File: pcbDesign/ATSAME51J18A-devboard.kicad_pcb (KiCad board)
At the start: 2 copper layers, 68 parts, among them J1 Micro_SD_Card, J2 S2B-ZR-SM4A-TF(LF)(SN), J3 SM04B-SRSS-TB(LF)(SN), J4 Conn_01x25, J5 Conn_01x01_Male, J6 Conn_01x02_Male, J7 Conn_01x06_Male, J8 Conn_01x25, J9 12401598E4-2A, U1 TCAN1051GVDRQ1, U2 ATSAME51J18A-A, U3 MIC5219-5.0YMM, U4 LM27762, U5 LM2775QDSGTQ1, U6 SC630AULTRT, U7 BQ24074RGT, U8 BQ27441DRZR-G1B, Y1 32.768

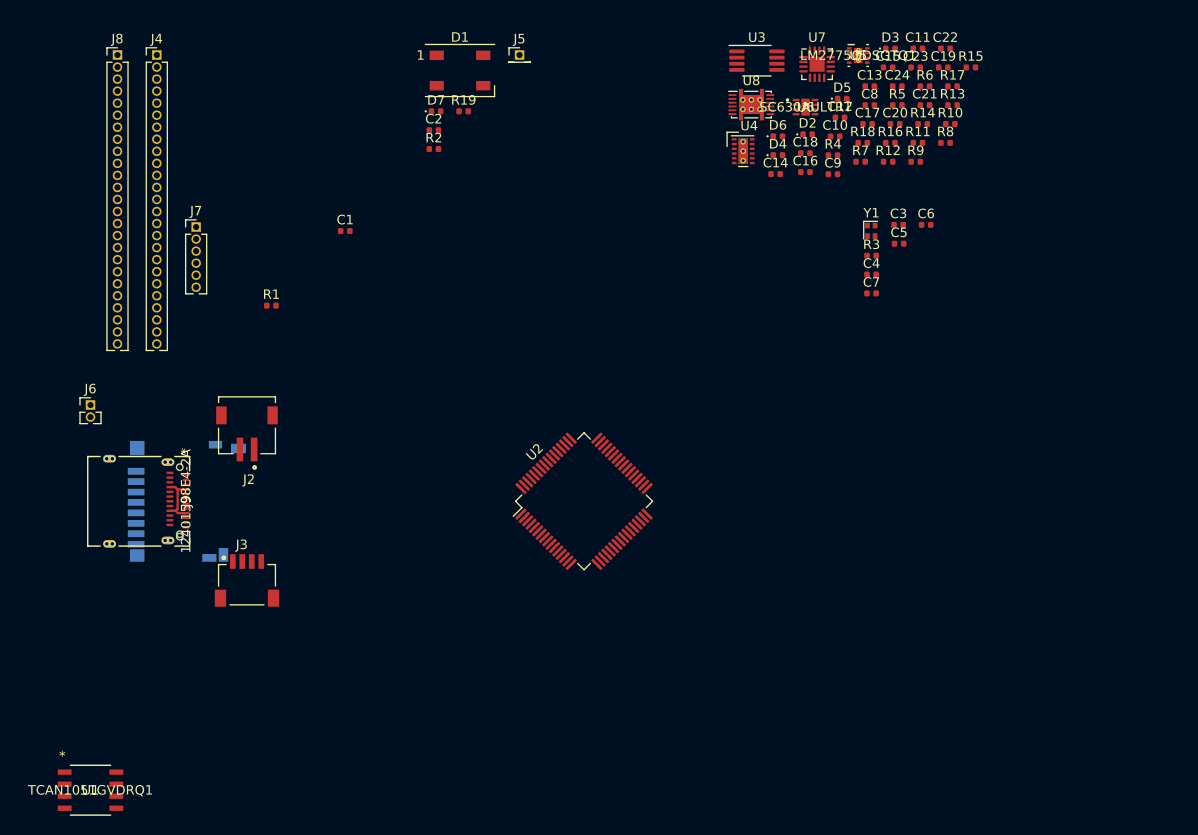
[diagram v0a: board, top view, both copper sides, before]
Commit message: Fixed power rail enabling systems and rearanged pins for easier use
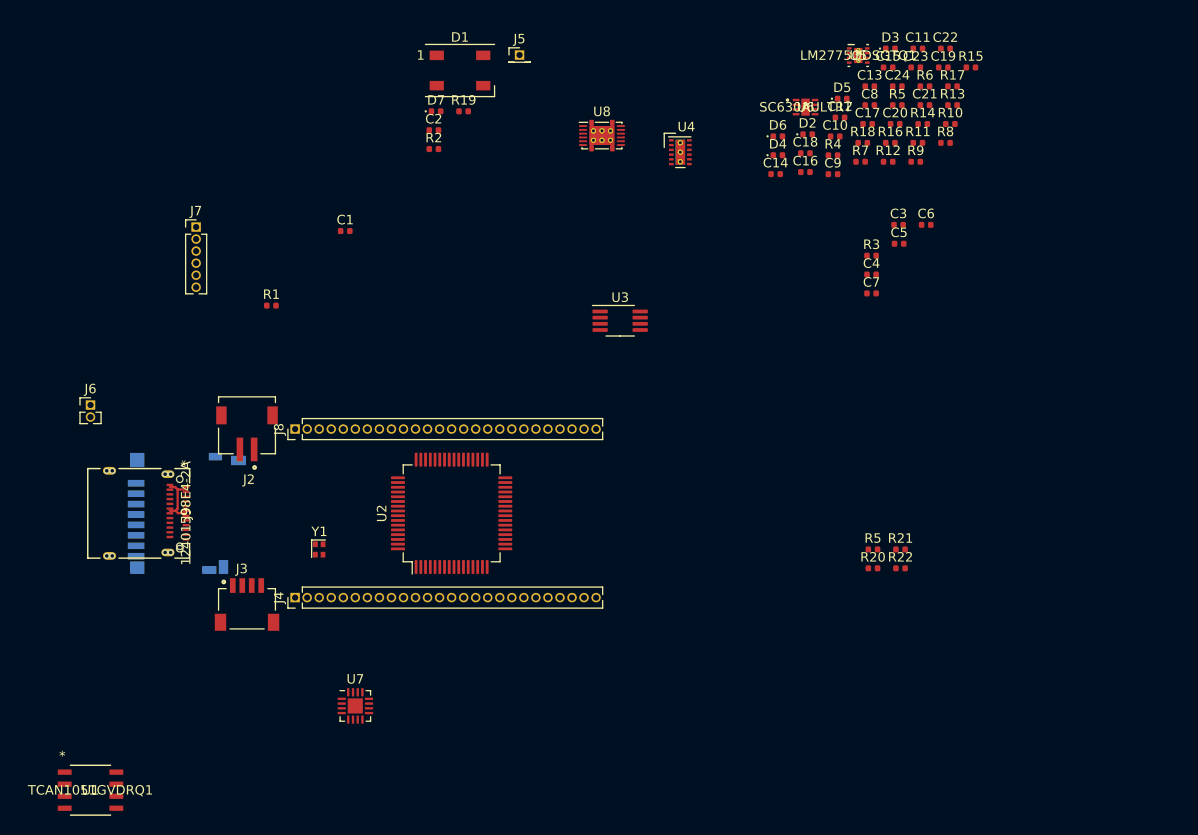
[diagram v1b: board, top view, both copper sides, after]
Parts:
- added R20: 10k, Resistor_SMD:R_0402_1005Metric, F.Cu at (193.0, 132.8)
- added R21: 10k, Resistor_SMD:R_0402_1005Metric, F.Cu at (195.9, 130.8)
- added R22: 10k, Resistor_SMD:R_0402_1005Metric, F.Cu at (195.9, 132.8)
- added R5: 10k, Resistor_SMD:R_0402_1005Metric, F.Cu at (193.0, 130.8)
- C17, C21: value C -> 2.2u
- J2: value S2B-ZR-SM4A-TF(LF)(SN) -> BAT
- J3: value SM04B-SRSS-TB(LF)(SN) -> QWIIC
- J4: value Conn_01x25 -> L_PINS; footprint Connector_PinHeader_1.27mm:PinHeader_1x25_P1.27mm_Vertical -> Connector_PinHeader_1.27mm:PinHeader_1x26_P1.27mm_Vertical
- J5: value Conn_01x01_Male -> NP_OUT
- J6: value Conn_01x02_Male -> USB
- J7: value Conn_01x06_Male -> QSPI
- J8: value Conn_01x25 -> R_PINS; footprint Connector_PinHeader_1.27mm:PinHeader_1x25_P1.27mm_Vertical -> Connector_PinHeader_1.27mm:PinHeader_1x26_P1.27mm_Vertical
- U2: value ATSAME51J18A-A -> ATSAME51JXXA-A
- moved U7 83.4 mm to (138.4, 147.3)
- moved Y1 67.2 mm to (134.6, 130.8)
- moved J4 59.1 mm to (132.1, 135.9), turned to 90 degrees
- moved J8 43.7 mm to (132.1, 118.1), turned to 90 degrees
- moved U3 31.0 mm to (166.4, 106.7)
- moved U8 16.1 mm to (164.4, 87.1)
- moved U2 14.0 mm to (148.6, 127.0), turned to 90 degrees
- moved U4 6.63 mm to (172.7, 88.9)
- moved J3 2.54 mm to (127.0, 134.6)
- moved J1 1.27 mm to (120.7, 127.0)
- moved J9 1.27 mm to (115.6, 127.0)
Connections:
- J4 pad 10: 7[I2SWS] -> 6[I2SSCK]
- J4 pad 11: 10[I2SDO] -> 7[I2SWS]
- J4 pad 12: 11[I2SDI] -> 10[I2SDO]
- J4 pad 13: 14[I2SMCLK] -> 11[I2SDI]
- J4 pad 14: 15 -> 14[I2SMCLK]
- J4 pad 15: 18 -> 15
- J4 pad 16: 19 -> 18
- J4 pad 17: 22 -> 19
- J4 pad 18: 23 -> 22
- J4 pad 19: 26 -> 23
- J4 pad 2: RST -> GND
- J4 pad 20: 27 -> 26
- J4 pad 21: 30[Rx1] -> 27
- J4 pad 22: 31[Tx1] -> 30[Rx1]
- J4 pad 23: VBUS_3V3_CH1_REG -> 31[Tx1]
- J4 pad 24: GND -> VBUS_3V3_CH1_REG
- J4 pad 25: VBUS_-3V3_CH2_REG -> GND
- J4 pad 3: CHRG -> RST
- J4 pad 4: VBUS_3V3_CH1_REG -> CHRG
- J4 pad 5: GND -> VBUS_3V3_CH1_REG
- J4 pad 6: VBUS_-3V3_CH2_REG -> GND
- J4 pad 7: 2[SDA] -> VBUS_-3V3_CH2_REG
- J4 pad 8: 3[SCL] -> 2[SDA]
- J4 pad 9: 6[I2SSCK] -> 3[SCL]
- J8 pad 10: 5[MO] -> 4[SCK]
- J8 pad 11: 8[MI] -> 5[MO]
- J8 pad 12: 9[CS] -> 8[MI]
- J8 pad 13: 12 -> 9[CS]
- J8 pad 14: 13 -> 12
- J8 pad 15: 16 -> 13
- J8 pad 16: 17 -> 16
- J8 pad 17: 20 -> 17
- J8 pad 18: 21 -> 20
- J8 pad 19: 24 -> 21
- J8 pad 2: VBUS_VIN_NREG -> GND
- J8 pad 20: 25 -> 24
- J8 pad 21: 28[CANH] -> 25
- J8 pad 22: 29[CANL] -> 28[CANH]
- J8 pad 23: VBUS_3V3_CH1_REG -> 29[CANL]
- J8 pad 24: GND -> VBUS_3V3_CH1_REG
- J8 pad 25: VBUS_-3V3_CH2_REG -> GND
- J8 pad 3: AREF -> VBUS_VIN_NREG
- J8 pad 4: VBUS_3V3_CH1_REG -> AREF
- J8 pad 5: GND -> VBUS_3V3_CH1_REG
- J8 pad 6: VBUS_-3V3_CH2_REG -> GND
- J8 pad 7: 0[Rx0] -> VBUS_-3V3_CH2_REG
- J8 pad 8: 1[Tx0] -> 0[Rx0]
- J8 pad 9: 4[SCK] -> 1[Tx0]

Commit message: Changed pin pitch to 2.54mm
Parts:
- removed the R5 at (195.6, 83.9)
- added J10: CAN, SM04B-SRSS-TB_LF__SN_:JST_SM04B-SRSS-TB(LF)(SN), F.Cu at (135.9, 134.6)
- J4, J8: footprint Connector_PinHeader_1.27mm:PinHeader_1x26_P1.27mm_Vertical -> Connector_PinSocket_2.54mm:PinSocket_1x26_P2.54mm_Vertical
- J5: footprint Connector_PinHeader_1.27mm:PinHeader_1x01_P1.27mm_Vertical -> Connector_PinSocket_2.54mm:PinSocket_1x01_P2.54mm_Vertical
- J6: footprint Connector_PinHeader_1.27mm:PinHeader_1x02_P1.27mm_Vertical -> Connector_PinSocket_2.54mm:PinSocket_1x02_P2.54mm_Vertical
- J7: footprint Connector_PinHeader_1.27mm:PinHeader_1x06_P1.27mm_Vertical -> Connector_PinSocket_2.54mm:PinSocket_1x06_P2.54mm_Vertical
- U2: value ATSAME51JXXA-A -> ATSAME51J18A-A
- moved J4 10.2 mm to (142.2, 135.9)
- moved J8 10.2 mm to (142.2, 118.1)
- moved J2 8.89 mm to (135.9, 118.1)
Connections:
- D6 pad 2: VBUS_BAT_NREG -> (no net)
- J4 pad 10: 6[I2SSCK] -> (no net)
- J4 pad 11: 7[I2SWS] -> (no net)
- J4 pad 15: 15 -> (no net)
- J4 pad 22: 30[Rx1] -> (no net)
- J4 pad 23: 31[Tx1] -> (no net)
- J9 pad A10: Net-(J9-PadA10) -> (no net)
- J9 pad A11: Net-(J9-PadA11) -> (no net)
- J9 pad A2: Net-(J9-PadA2) -> (no net)
- J9 pad A3: Net-(J9-PadA3) -> (no net)
- J9 pad A8: Net-(J9-PadA8) -> (no net)
- J9 pad B10: Net-(J9-PadB10) -> (no net)
- J9 pad B11: Net-(J9-PadB11) -> (no net)
- J9 pad B2: Net-(J9-PadB2) -> (no net)
- J9 pad B3: Net-(J9-PadB3) -> (no net)
- J9 pad B8: Net-(J9-PadB8) -> (no net)
- U2 pad 15: SDCD -> (no net)
- U2 pad 16: SDWP -> (no net)
- U2 pad 3: 30 -> (no net)
- U2 pad 39: 6[I2SCK] -> (no net)
- U2 pad 41: 15[I2SFS] -> (no net)
- U2 pad 44: 31 -> (no net)
- U2 pad 55: Net-(U2-Pad55) -> (no net)
- U2 pad 57: SWCLK -> (no net)
- U2 pad 58: SWDIO -> (no net)
- U2 pad 59: SWO -> (no net)
- U7 pad 1: Net-(U7-Pad1) -> (no net)
- U7 pad 15: Net-(U7-Pad15) -> (no net)
- U7 pad 7: Net-(U7-Pad7) -> (no net)

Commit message: Finnished routing
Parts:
- added D8: PWR, LED_SMD:LED_0402_1005Metric, F.Cu at (153.7, 127.0)
- added D9: CHRG, LED_SMD:LED_0402_1005Metric, F.Cu at (153.7, 126.0)
- added R23: 10k, Resistor_SMD:R_0402_1005Metric, F.Cu at (155.7, 127.0)
- added R24: 10k, Resistor_SMD:R_0402_1005Metric, F.Cu at (155.7, 126.0)
- C10, C11, C12, C13, C14, C15, C16, C17, C18, C19, C20, C21, C22, C23, C24, C8, C9, D2, D3, D5, J10, J3, R10, R11, R12, R13, R14, R15, R16, R17, R18, R20, R21, R22, R4, R5, R6, R7, R8, R9, U3, U4, U5, U6, U7, U8: moved to B.Cu
- J1: moved to F.Cu
- J9: value 12401598E4-2A -> USB4105_REVA; footprint usb_c:12401598E4-2A -> USB4105_REVA:GCT_USB4105_REVA
- Y1: footprint Oscillator:Oscillator_SMD_Abracon_ASCO-4Pin_1.6x1.2mm -> Crystal:Crystal_SMD_2012-2Pin_2.0x1.2mm
- moved J6 97.9 mm to (206.2, 136.1), turned to 270 degrees
- moved U1 84.1 mm to (187.2, 121.7), turned to 90 degrees
- moved J1 80.0 mm to (200.7, 127.0)
- moved J3 76.3 mm to (203.2, 131.1), turned to 270 degrees
- moved J7 75.0 mm to (193.5, 118.1), turned to 90 degrees
- moved C22 73.3 mm to (154.3, 134.7), turned to 270 degrees
- moved J5 73.3 mm to (201.2, 136.1), turned to 180 degrees
- moved J10 68.2 mm to (203.2, 123.4), turned to 270 degrees
- moved R13 67.8 mm to (150.5, 128.7), turned to 180 degrees
- moved R17 66.9 mm to (148.6, 122.9), turned to 180 degrees
- moved D3 65.7 mm to (158.9, 133.0)
- moved D1 64.6 mm to (187.7, 132.3), turned to 180 degrees
- moved R11 64.6 mm to (149.9, 131.2)
- moved C23 63.7 mm to (154.3, 126.7), turned to 90 degrees
- moved R15 62.2 mm to (156.8, 121.2)
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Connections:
- net GPOUT_PIN renamed VBUS_3V3_CH0_REG
- net USB_DM renamed USB_N
- net USB_DP renamed USB_P
- C22 pad 1: Net-(C22-Pad1) -> VBUS_BAT_NREG
- D6 pad 2: (no net) -> VBUS_BAT_NREG
- J4 pad 10: (no net) -> 6[I2SSCK]
- J4 pad 11: (no net) -> 7[I2SWS]
- J4 pad 15: (no net) -> 15
- J4 pad 22: (no net) -> 30
- J4 pad 23: (no net) -> 31
- R1 pad 1: Net-(J9-PadA5) -> GND
- R1 pad 2: GND -> Net-(J9-PadA5)
- R19 pad 1: LED_PIN -> 13
- U2 pad 26: 13 -> 15
- U2 pad 3: (no net) -> 30
- U2 pad 39: (no net) -> 6[I2SSCK]
- U2 pad 41: (no net) -> 7[I2SWS]
- U2 pad 44: (no net) -> 31
- U2 pad 60: LED_PIN -> 13
- U7 pad 10: Net-(C22-Pad1) -> VBUS_BAT_NREG
- U7 pad 11: Net-(C22-Pad1) -> VBUS_BAT_NREG
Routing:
- net GND: track 0.00 -> 408.1 mm, vias 0 -> 28
- net VBUS_3V3_CH0_REG: track 0.00 -> 156.7 mm, vias 0 -> 5
- net VBUS_3V3_CH1_REG: track 0.00 -> 142.2 mm, vias 0 -> 2
- net VBUS_-3V3_CH2_REG: track 0.00 -> 128.0 mm, vias 0 -> 1
- net EN: track 0.00 -> 123.5 mm, vias 0 -> 3
- net USB_N: track 0.00 -> 121.8 mm, vias 0 -> 6
- net VBUS_NREG: track 0.00 -> 104.1 mm, vias 0 -> 9
- net 2[SDA]: track 0.00 -> 103.5 mm, vias 0 -> 6
- net 3[SCL]: track 0.00 -> 95.4 mm, vias 0 -> 3
- net USB_P: track 0.00 -> 89.6 mm, vias 0 -> 4
- net VBUS_VIN_NREG: track 0.00 -> 86.9 mm
- net 31: track 0.00 -> 57.3 mm, vias 0 -> 3
- net 0[Rx0]: track 0.00 -> 57.2 mm, vias 0 -> 5
- net QDAT2: track 0.00 -> 55.0 mm
- net QDAT1: track 0.00 -> 51.9 mm
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- added copper zone on B.Cu, net GND
- added copper zone on F.Cu, net GND
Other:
- board outline added: 67.3 x 29.2 mm
- net class Default: clearance 0.2 -> 0.127; trace_width 0.25 -> 0.2
- net class Power added: clearance 0.127, trace_width 0.4, via_dia 0.8, via_drill 0.4
- rule trace_clearance: 0.2 -> 0.127
- rule trace_min: 0.2 -> 0.127

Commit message: Labeled pins done
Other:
- board text added: "-3V3"
- board text added: "-3v3"
- board text added: "0"
- board text added: "1"
- board text added: "10"
- board text added: "11"
- board text added: "12"
- board text added: "13"
- board text added: "14"
- board text added: "15"
- board text added: "16"
- board text added: "17"
- board text added: "18"
- board text added: "19"
- board text added: "2"
- board text added: "20"
- board text added: "21"
- board text added: "22"
- board text added: "23"
- board text added: "24"
- board text added: "25"
- board text added: "26"
- board text added: "27"
- board text added: "28"
- board text added: "29"
- board text added: "3"
- board text added: "30"
- board text added: "31"
- board text added: "3V3"
- board text added: "4"
- board text added: "5"
- board text added: "6"
- board text added: "7"
- board text added: "8"
- board text added: "9"
- board text added: "AREF"
- board text added: "BAT"
- board text added: "CANH"
- board text added: "CANL"
- board text added: "CHRG"
- board text added: "CS"
- board text added: "EN"
- board text added: "GND"
- board text added: "I2SDI"
- board text added: "I2SDO"
- board text added: "I2SMCLK"
- board text added: "I2SSCK"
- board text added: "I2SWS"
- board text added: "MI"
- board text added: "MO"
- board text added: "NPO"
- board text added: "QCS"
- board text added: "QD0"
- board text added: "QD1"
- board text added: "QD2"
- board text added: "QD3"
- board text added: "QSCK"
- board text added: "RST"
- board text added: "RX"
- board text added: "SCK"
- board text added: "SCL"
- board text added: "SDA"
- board text added: "TX"
- board text added: "USB+"
- board text added: "USB-"
- board text added: "VIN"

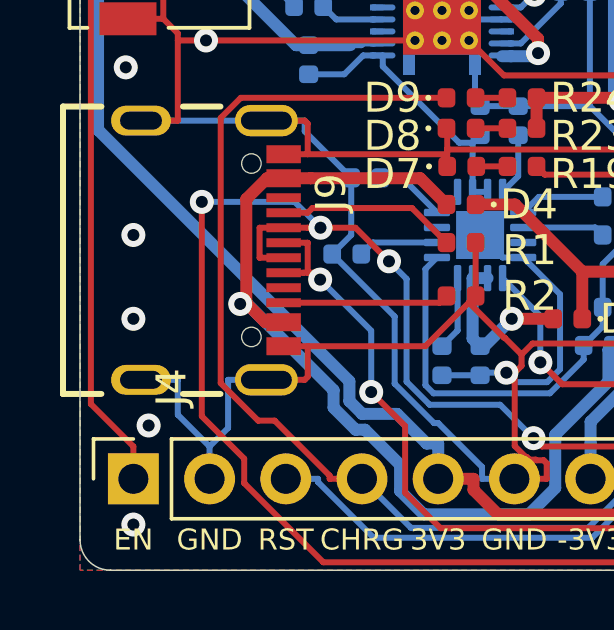
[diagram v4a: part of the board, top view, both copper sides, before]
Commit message: Repanelized board after adding pin descriptions
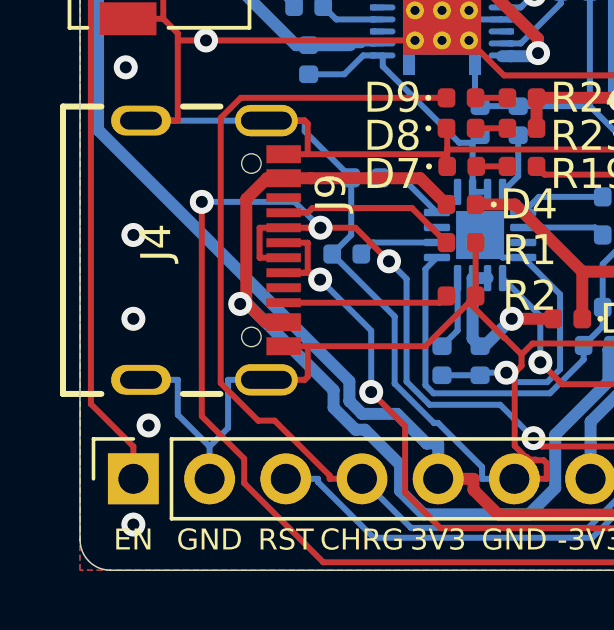
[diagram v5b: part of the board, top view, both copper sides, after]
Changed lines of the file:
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@@
-(kicad_pcb (version 20171130) (host pcbnew "(5.1.6)-1")
+(kicad_pcb (version 20171130) (host pcbnew 5.1.5+dfsg1-2build2)
   (general
     (thickness 1.6)
@@
   (page A4)
   (layers
-    (0 F.Cu signal)
-    (31 B.Cu signal)
+    (0 F.Cu signal hide)
+    (31 B.Cu signal hide)
     (32 B.Adhes user)
     (33 F.Adhes user)
@@
     (descr "Through hole straight socket strip, 1x26, 2.54mm pitch, single row (from Kicad 4.0.7), script generated")
     (tags "Through hole socket strip THT 1x26 2.54mm single row")
-    (fp_text reference J4 (at 3.048 1.27 90) (layer F.SilkS)
-      (effects (font (size 1 1) (thickness 0.15)))
-    )
+    (fp_text reference J4 (at 7.874 0.762 90) (layer F.SilkS)
+      (effects (font (size 1 1) (thickness 0.15)))
+    )

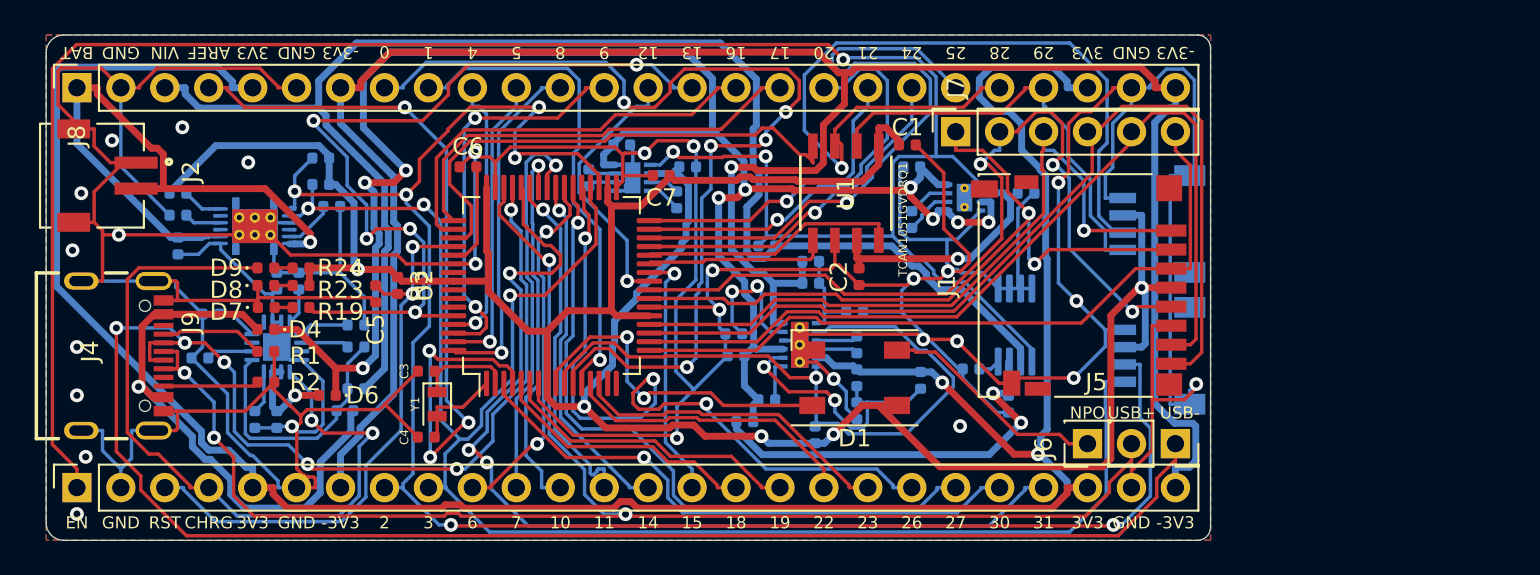
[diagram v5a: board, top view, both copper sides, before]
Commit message: Changed the layout of pins to make room for SWD and made the board longer
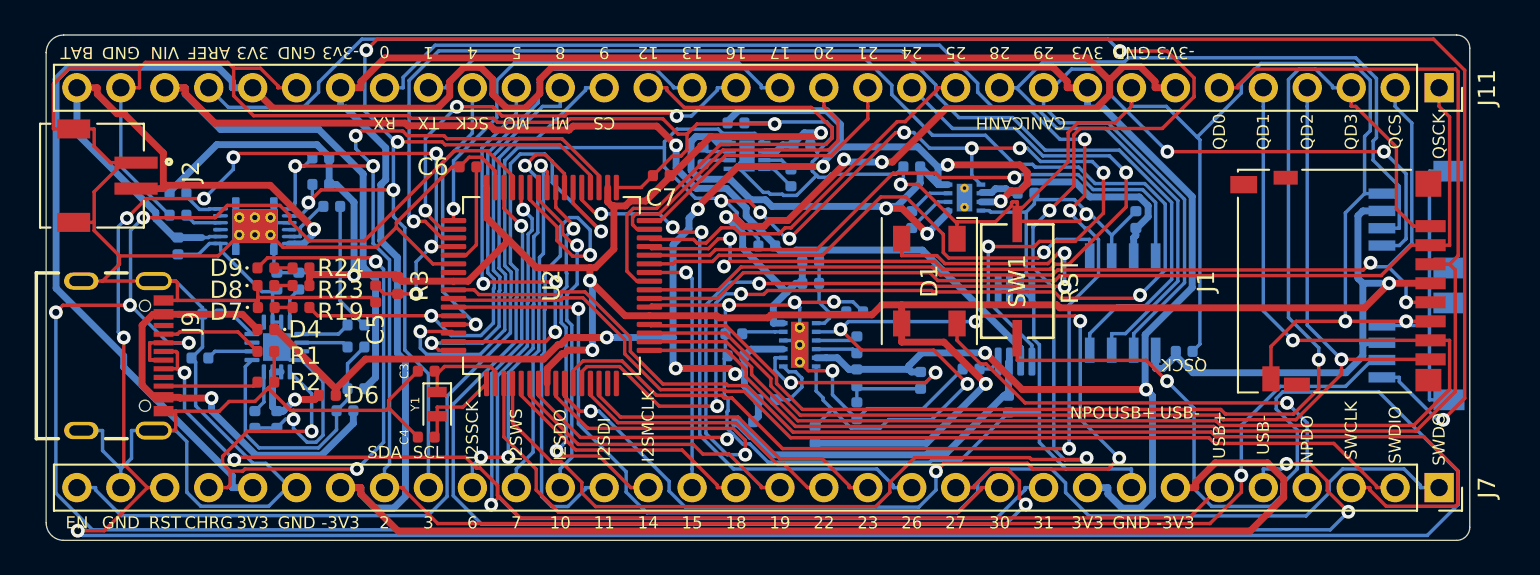
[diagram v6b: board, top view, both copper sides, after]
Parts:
- removed J4: L_PINS, Connector_PinSocket_2.54mm:PinSocket_1x26_P2.54mm_Vertical
- removed J5: NP_OUT, Connector_PinSocket_2.54mm:PinSocket_1x01_P2.54mm_Vertical
- removed J6: USB, Connector_PinSocket_2.54mm:PinSocket_1x02_P2.54mm_Vertical
- removed J8: R_PINS, Connector_PinSocket_2.54mm:PinSocket_1x26_P2.54mm_Vertical
- added J11: Conn_01x32_Male, Connector_PinSocket_2.54mm:PinSocket_1x32_P2.54mm_Vertical, F.Cu at (221.5, 115.6)
- added SW1: RST, PTS636:PTS636 SM25F SMTR LFS, F.Cu at (197.1, 126.7)
- C1, C2, U1: moved to B.Cu
- J7: value QSPI -> Conn_01x32_Male; footprint Connector_PinSocket_2.54mm:PinSocket_1x06_P2.54mm_Vertical -> Connector_PinSocket_2.54mm:PinSocket_1x32_P2.54mm_Vertical
- moved J7 34.7 mm to (221.5, 138.7), turned to 270 degrees
- moved C1 20.0 mm to (206.8, 130.8)
- moved U1 17.2 mm to (203.2, 128.0), turned to 270 degrees
- moved C2 16.3 mm to (204.0, 123.2), turned to 270 degrees
- moved J10 15.0 mm to (218.2, 123.2)
- moved J3 15.0 mm to (218.2, 130.8)
- moved J1 15.0 mm to (215.6, 126.7)
- moved D1 7.06 mm to (192.0, 126.7), turned to 90 degrees
- moved C20 6.73 mm to (180.8, 117.6)
- moved C21 6.73 mm to (178.9, 119.5)
- moved U6 6.73 mm to (181.5, 119.5)
- moved C17 6.73 mm to (184.0, 120.8)
- moved C19 6.73 mm to (184.7, 118.9)
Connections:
- J7 pad 1: QSCK -> SWDO
- J7 pad 2: QCS -> SWDIO
- J7 pad 3: QDAT3 -> SWCLK
- J7 pad 4: QDAT2 -> NEOPIXEL_DOUT
- J7 pad 5: QDAT1 -> USB_N
- J7 pad 6: QDAT0 -> USB_P
- U2 pad 57: (no net) -> SWCLK
- U2 pad 58: (no net) -> SWDIO
- U2 pad 59: (no net) -> SWDO
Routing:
- net RST: track 33.4 -> 179.5 mm, vias 2 -> 9
- net AREF: track 46.8 -> 130.5 mm, vias 4 -> 3
- net SWCLK: track 0.00 -> 71.7 mm
- net SWDO: track 0.00 -> 71.3 mm, vias 0 -> 1
- net 1[Tx0]: track 28.5 -> 93.8 mm, vias 1 -> 3
- net SWDIO: track 0.00 -> 59.6 mm
- net GND: track 408.1 -> 464.8 mm, vias 28 -> 11
- net VBUS_-3V3_CH2_REG: track 128.0 -> 183.7 mm, vias 1 -> 3
- net EN_2: track 39.4 -> 84.7 mm, vias 1 -> 7
- net QDAT0: track 41.8 -> 84.0 mm
- net 3[SCL]: track 95.4 -> 137.6 mm, vias 3 -> 5
- net CAN_S: track 29.4 -> 71.1 mm, vias 0 -> 1
- net 0[Rx0]: track 57.2 -> 95.8 mm, vias 5 -> 3
- net NEOPIXEL_DIN: track 19.7 -> 58.0 mm, vias 2 -> 4
- net 27: track 39.6 -> 72.3 mm, vias 1 -> 2
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- removed copper zone on B.Cu, net GND
- removed copper zone on F.Cu, net GND
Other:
- board size 67.3 x 29.2 mm -> 82.3 x 29.2 mm
- board text added: "NPDO"
- board text added: "SWCLK"
- board text added: "SWDIO"
- board text added: "SWDO"
